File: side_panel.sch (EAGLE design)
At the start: 35 parts

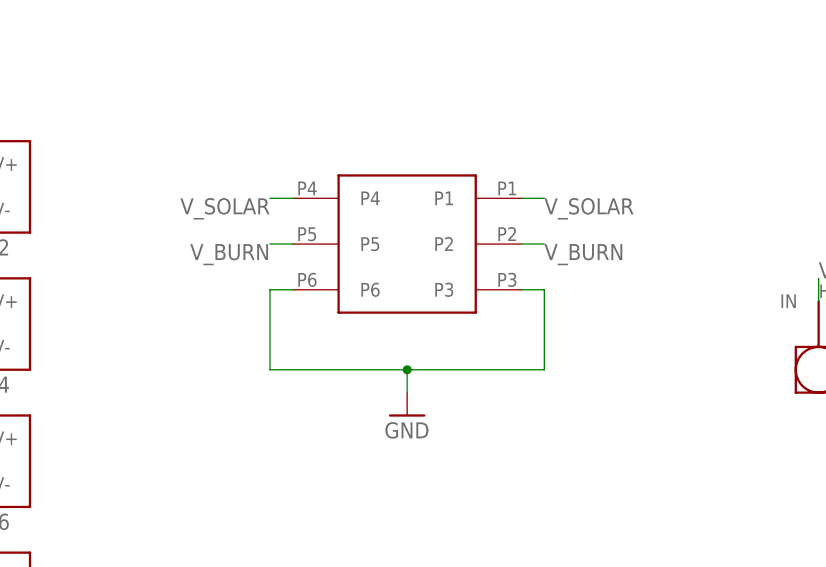
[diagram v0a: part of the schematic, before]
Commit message: Updated side panel connectors
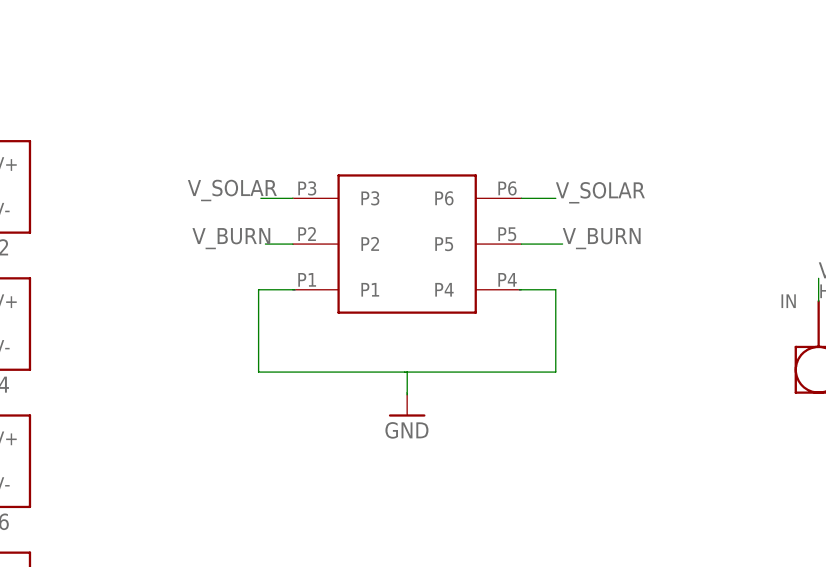
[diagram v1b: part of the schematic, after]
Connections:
- net GND: no longer U$1.P3, U$1.P6
- net V_SOLAR: now also U$1.P3, U$1.P6; no longer U$1.P1, U$1.P4
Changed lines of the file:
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@@
 <attribute name="NAME" x="79.375" y="78.994" size="1.778" layer="95" rot="R90"/>
 </instance>
-<instance part="U$1" gate="G$1" x="140.97" y="62.23" rot="R270"/>
+<instance part="U$1" gate="G$1" x="140.97" y="62.23" rot="R90"/>
 <instance part="GND4" gate="1" x="195.58" y="35.56"/>
 <instance part="GND5" gate="1" x="140.97" y="43.18"/>
@@
 </segment>
 <segment>
-<pinref part="U$1" gate="G$1" pin="P1"/>
-<wire x1="153.67" y1="67.31" x2="156.21" y2="67.31" width="0.1524" layer="91"/>
-<label x="156.21" y="67.31" size="1.778" layer="95" rot="MR180"/>
-</segment>
-<segment>
-<pinref part="U$1" gate="G$1" pin="P4"/>
-<wire x1="128.27" y1="67.31" x2="125.73" y2="67.31" width="0.1524" layer="91"/>
-<label x="125.73" y="67.31" size="1.778" layer="95" rot="R180"/>
+<pinref part="U$1" gate="G$1" pin="P3"/>
+<wire x1="128.27" y1="67.31" x2="124.714" y2="67.31" width="0.1524" layer="91"/>
+<label x="116.586" y="67.564" size="1.778" layer="95"/>
+</segment>
+<segment>
+<pinref part="U$1" gate="G$1" pin="P6"/>
+<wire x1="153.67" y1="67.31" x2="157.48" y2="67.31" width="0.1524" layer="91"/>
+<label x="157.48" y="67.31" size="1.778" layer="95"/>
 </segment>
 </net>
@@
 </segment>
 <segment>
-<pinref part="U$1" gate="G$1" pin="P6"/>
-<wire x1="128.27" y1="57.15" x2="125.73" y2="57.15" width="0.1524" layer="91"/>
-<wire x1="125.73" y1="57.15" x2="125.73" y2="48.26" width="0.1524" layer="91"/>
-<pinref part="U$1" gate="G$1" pin="P3"/>
-<wire x1="153.67" y1="57.15" x2="156.21" y2="57.15" width="0.1524" layer="91"/>
-<wire x1="125.73" y1="48.26" x2="140.97" y2="48.26" width="0.1524" layer="91"/>
-<wire x1="140.97" y1="48.26" x2="156.21" y2="48.26" width="0.1524" layer="91"/>
-<wire x1="156.21" y1="48.26" x2="156.21" y2="57.15" width="0.1524" layer="91"/>
-<pinref part="GND5" gate="1" pin="GND"/>
-<wire x1="140.97" y1="45.72" x2="140.97" y2="48.26" width="0.1524" layer="91"/>
-<junction x="140.97" y="48.26"/>
+<wire x1="140.97" y1="45.466" x2="140.97" y2="48.006" width="0.1524" layer="91"/>
+<wire x1="140.97" y1="48.006" x2="140.716" y2="48.006" width="0.1524" layer="91"/>
+<wire x1="140.716" y1="48.006" x2="124.46" y2="48.006" width="0.1524" layer="91"/>
+<wire x1="124.46" y1="48.006" x2="124.46" y2="57.15" width="0.1524" layer="91"/>
+<wire x1="124.46" y1="57.15" x2="128.524" y2="57.15" width="0.1524" layer="91"/>
+<wire x1="153.416" y1="57.15" x2="157.48" y2="57.15" width="0.1524" layer="91"/>
+<wire x1="157.48" y1="57.15" x2="157.48" y2="48.006" width="0.1524" layer="91"/>
+<wire x1="157.48" y1="48.006" x2="140.97" y2="48.006" width="0.1524" layer="91"/>
 </segment>
 </net>
@@
 <net name="V_BURN" class="0">
 <segment>
-<pinref part="U$1" gate="G$1" pin="P5"/>
-<wire x1="128.27" y1="62.23" x2="125.73" y2="62.23" width="0.1524" layer="91"/>
-<label x="125.73" y="62.23" size="1.778" layer="95" rot="R180"/>
-</segment>
-<segment>
-<pinref part="U$1" gate="G$1" pin="P2"/>
-<wire x1="153.67" y1="62.23" x2="156.21" y2="62.23" width="0.1524" layer="91"/>
-<label x="156.21" y="62.23" size="1.778" layer="95" rot="MR180"/>
-</segment>
-<segment>
 <wire x1="186.69" y1="55.88" x2="186.69" y2="58.42" width="0.1524" layer="91"/>
 <label x="186.69" y="58.42" size="1.778" layer="95"/>
 <pinref part="U$4" gate="G$1" pin="IN"/>
 </segment>
-</net>
+<segment>
+<pinref part="U$1" gate="G$1" pin="P5"/>
+<wire x1="153.67" y1="62.23" x2="158.242" y2="62.23" width="0.1524" layer="91"/>
+<label x="158.242" y="62.23" size="1.778" layer="95"/>
+</segment>
+<segment>
+<pinref part="U$1" gate="G$1" pin="P2"/>
+<wire x1="128.27" y1="62.23" x2="125.222" y2="62.23" width="0.1524" layer="91"/>
+<label x="117.094" y="62.23" size="1.778" layer="95"/>
+</segment>
+</net>
